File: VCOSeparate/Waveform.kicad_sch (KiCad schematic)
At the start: 27 parts, among them Q1 Q_NPN_ECB, U1 Opamp_Dual, U2 4013, U3 Opamp_Dual

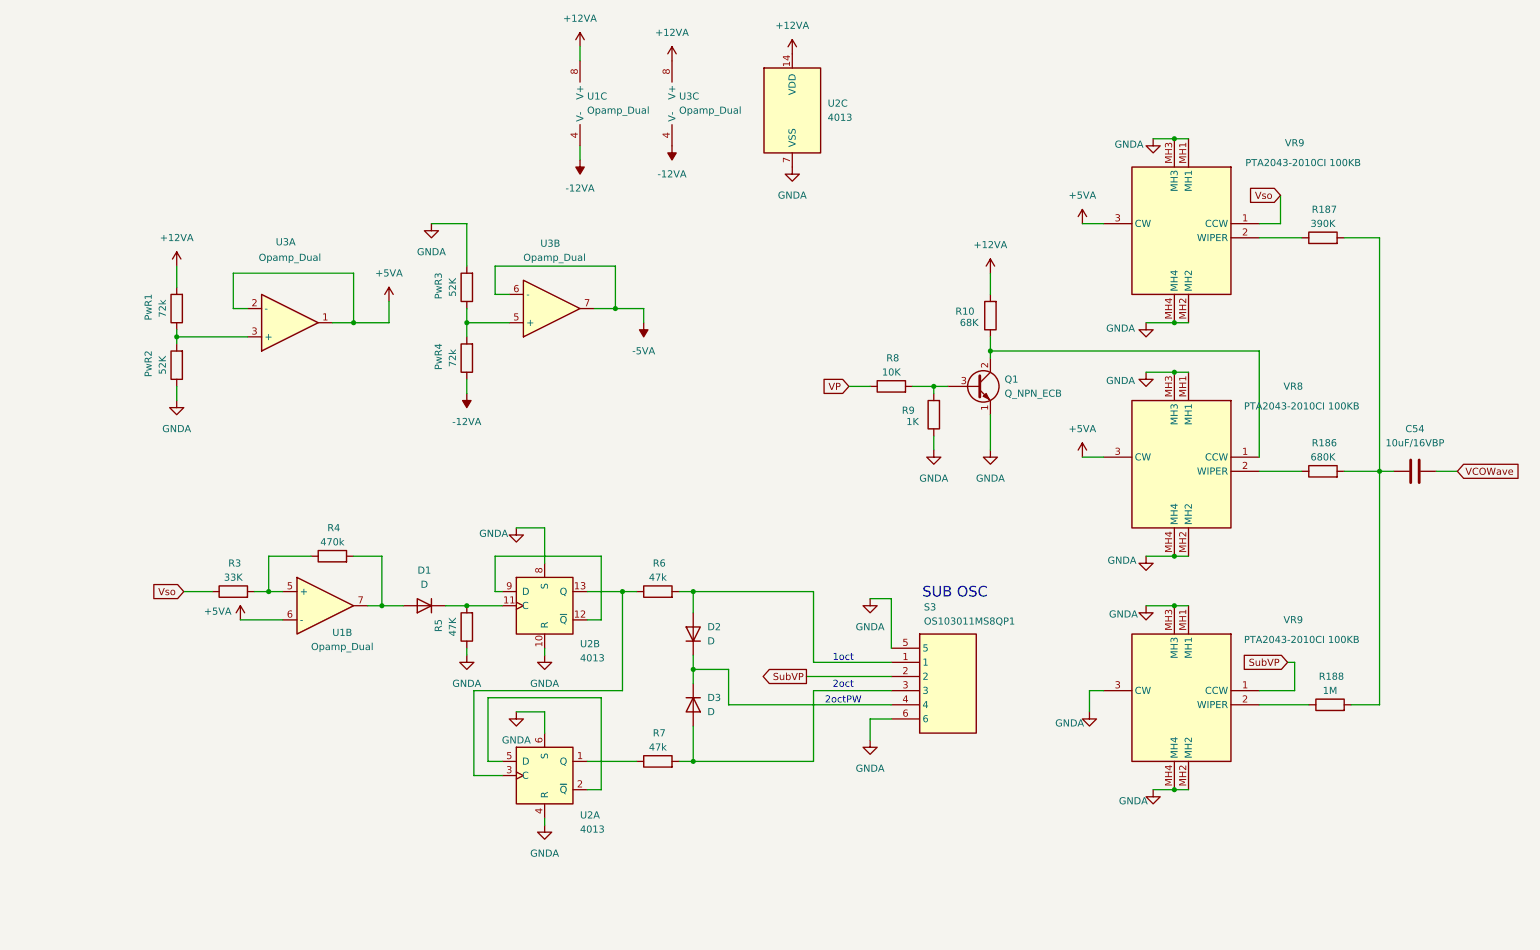
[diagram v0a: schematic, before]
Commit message: MC2
アクセントレベルを追加したEGACCを登録
回路全般部品配置済
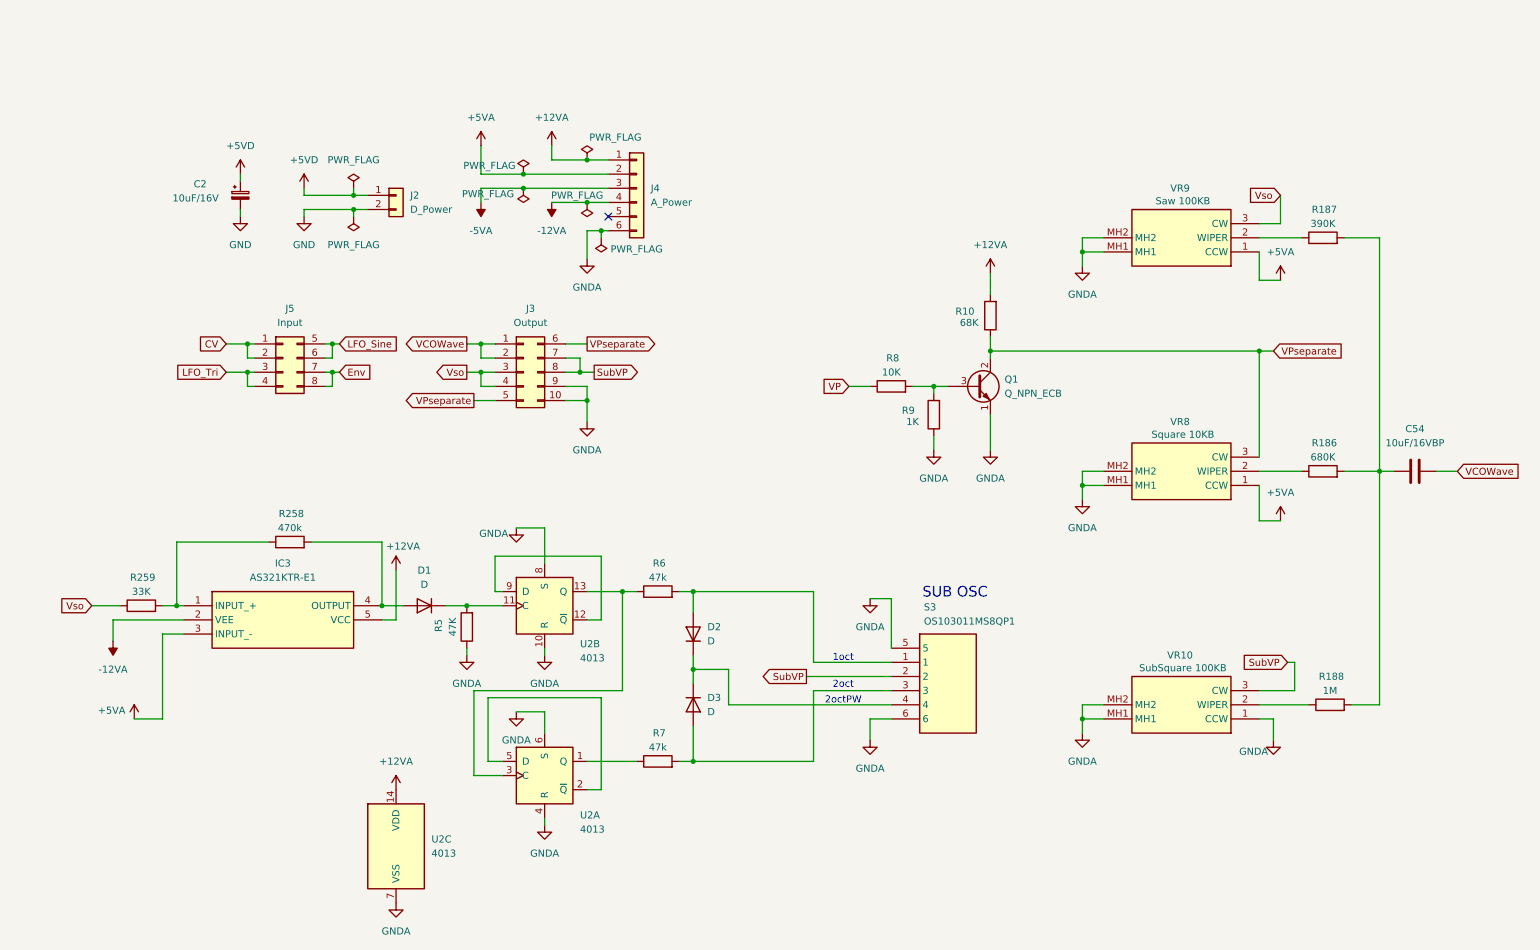
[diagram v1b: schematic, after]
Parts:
- removed PwR1, PwR4: 72k, Resistor_THT:R_Axial_DIN0207_L6.3mm_D2.5mm_P2.54mm_Vertical, symbol Device:R
- removed PwR2, PwR3: 52K, Resistor_THT:R_Axial_DIN0207_L6.3mm_D2.5mm_P2.54mm_Vertical, symbol Device:R
- removed R3: 33K, Resistor_THT:R_Axial_DIN0207_L6.3mm_D2.5mm_P2.54mm_Vertical, symbol Device:R
- removed R4: 470k, Resistor_THT:R_Axial_DIN0207_L6.3mm_D2.5mm_P2.54mm_Vertical, symbol Device:R
- removed U1, U3: Opamp_Dual, Package_DIP:DIP-8_W7.62mm_LongPads, symbol Device:Opamp_Dual
- removed VR8, VR9 (x2): PTA2043-2010CI 100KB, PTA20432010CIB104, symbol SamacSys_Parts:PTA2043-2010CIB104
- added C2: 10uF/16V, Capacitor_THT:CP_Radial_D5.0mm_P2.50mm, symbol Device:C_Polarized_Small
- added IC3: AS321KTR-E1, SOT95P282X145-5N, symbol SamacSys_Parts:AS321KTR-E1
- added J2: D_Power, Connector_PinSocket_2.54mm:PinSocket_1x02_P2.54mm_Vertical, symbol Connector_Generic:Conn_01x02
- added J3: Output, Connector_PinSocket_2.54mm:PinSocket_2x05_P2.54mm_Vertical, symbol Connector_Generic:Conn_02x05_Top_Bottom
- added J4: A_Power, Connector_PinHeader_2.54mm:PinHeader_1x06_P2.54mm_Vertical, symbol Connector_Generic:Conn_01x06
- added J5: Input, Connector_PinSocket_2.54mm:PinSocket_2x04_P2.54mm_Vertical, symbol Connector_Generic:Conn_02x04_Top_Bottom
- added R258: 470k, Resistor_THT:R_Axial_DIN0207_L6.3mm_D2.5mm_P2.54mm_Vertical, symbol Device:R
- added R259: 33K, Resistor_THT:R_Axial_DIN0207_L6.3mm_D2.5mm_P2.54mm_Vertical, symbol Device:R
- added VR10: SubSquare 100KB, SamacSys_Parts:RK09D117000B, symbol SamacSys_Parts:RK09D117000B
- added VR8: Square 10KB, SamacSys_Parts:RK09D117000B, symbol SamacSys_Parts:RK09D117000B
- added VR9: Saw 100KB, SamacSys_Parts:RK09D117000B, symbol SamacSys_Parts:RK09D117000B
- Q1: footprint (none) -> Package_TO_SOT_THT:TO-92_HandSolder
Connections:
- net +12VA: now also IC3.5 (VCC), J4.1 (Pin_1)
- net +5VA: now also IC3.3 (INPUT_-), J4.2 (Pin_2), VR8.1 (CCW), VR9.1 (CCW)
- net -12VA: now also IC3.2 (VEE), J4.4 (Pin_4)
- net -5VA: now also J4.3 (Pin_3)
- net GNDA: now also J3.10 (Pin_10), J3.9 (Pin_9), J4.6 (Pin_6), VR10.1 (CCW), VR10.MH1, VR10.MH2, VR8.MH1, VR8.MH2, VR9.MH1, VR9.MH2
- net SubVP: now also J3.7 (Pin_7), J3.8 (Pin_8), VR10.3 (CW)
- net VCOWave: now also J3.1 (Pin_1), J3.2 (Pin_2)
- net Vso: now also J3.3 (Pin_3), J3.4 (Pin_4), R259.1, VR9.3 (CW)
- net at D1.2 (A): now also IC3.4 (OUTPUT), R258.2
- net VPseparate: now reaches Q1.2 (C), R10.1
- net VPseparate: now also J3.5 (Pin_5), J3.6 (Pin_6), VR8.3 (CW)
- net at R186.1: now also VR8.2 (WIPER)
- net at R188.1: now also VR10.2 (WIPER)
- net at R187.1: now also VR9.2 (WIPER)
- new net: IC3.1 (INPUT_+), R258.1, R259.2
- new net +5VD: C2.1, J2.1 (Pin_1)
- new net CV: J5.1 (Pin_1), J5.2 (Pin_2)
- new net Env: J5.7 (Pin_7), J5.8 (Pin_8)
- new net GND: C2.2, J2.2 (Pin_2)
- new net LFO_Sine: J5.5 (Pin_5), J5.6 (Pin_6)
- new net LFO_Tri: J5.3 (Pin_3), J5.4 (Pin_4)
- no-connect marks 0 -> 1
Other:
- moved on the sheet: U2C

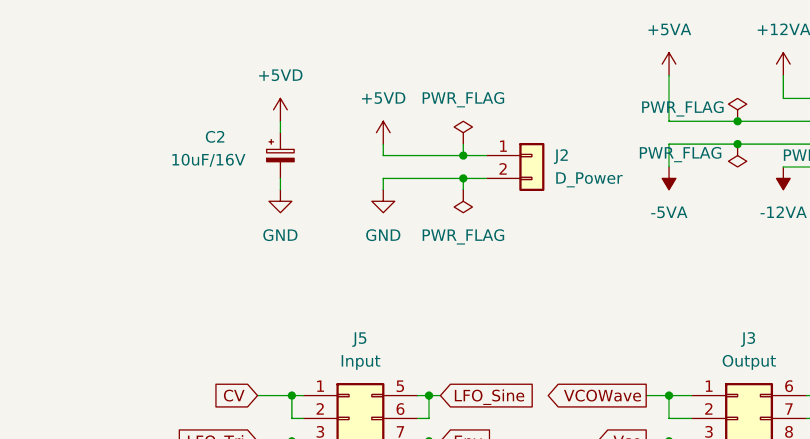
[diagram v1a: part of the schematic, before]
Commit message: MC2
VCO,VCF+VCA,Powerを登録
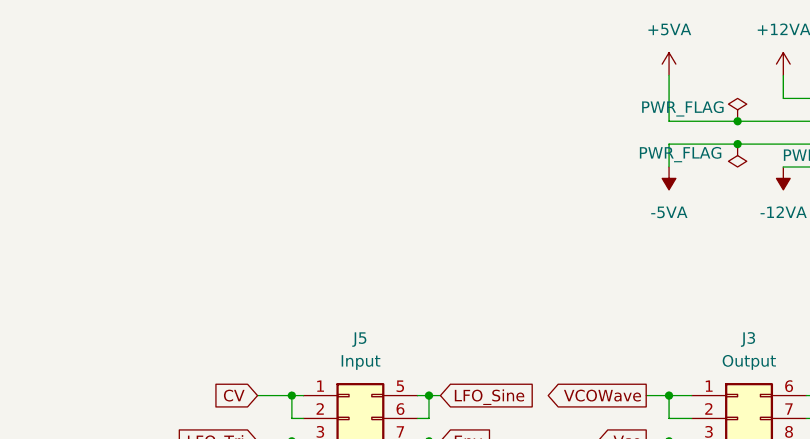
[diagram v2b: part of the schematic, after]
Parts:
- removed C2: 10uF/16V, Capacitor_THT:CP_Radial_D5.0mm_P2.50mm, symbol Device:C_Polarized_Small
- removed J2: D_Power, Connector_PinSocket_2.54mm:PinSocket_1x02_P2.54mm_Vertical, symbol Connector_Generic:Conn_01x02

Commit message: MC2
ここまででFIXした内容
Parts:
- removed Q1: Q_NPN_ECB, Package_TO_SOT_THT:TO-92_HandSolder, symbol Device:Q_NPN_ECB
- added Q18: Q_NPN_ECB, Package_TO_SOT_THT:TO-92_HandSolder, symbol Transistor_BJT:Q_NPN_ECB
- C54: footprint Capacitor_THT:C_Radial_D4.0mm_H7.0mm_P1.50mm -> Capacitor_THT:C_Radial_D6.3mm_H7.0mm_P2.50mm
- IC3: footprint SOT95P282X145-5N -> SamacSys_parts:SOT95P282X145-5N
- S3: footprint OS103011MS8QP1 -> SamacSys_parts:OS103011MS8QP1
- VR10, VR8, VR9: footprint SamacSys_Parts:RK09D117000B -> SamacSys_parts:RK09D117000B
- renumbered D1 to D28, D3 to D31, D2 to D32, U2 to IC4, R5 to R123, R10 to R124, R8 to R128, R9 to R129, R7 to R189, R6 to R190
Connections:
- net GNDA: now also Q18.1 (E)
- net VPseparate: now also Q18.2 (C)
- net at R128.2, R129.2: now also Q18.3 (B)

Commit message: MC2
デバッグ一通り完了して動作出来た
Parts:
- removed J3: Output, Connector_PinSocket_2.54mm:PinSocket_2x05_P2.54mm_Vertical, symbol Connector_Generic:Conn_02x05_Top_Bottom
- added J1: SyncIn, Connector_PinSocket_2.54mm:PinSocket_2x03_P2.54mm_Vertical, symbol Connector_Generic:Conn_02x03_Odd_Even
- added J2: Output, Connector_PinSocket_2.54mm:PinSocket_2x06_P2.54mm_Vertical, symbol Connector_Generic:Conn_02x06_Odd_Even
- added J3: LFM Wave, Connector_PinSocket_2.54mm:PinSocket_2x03_P2.54mm_Vertical, symbol Connector_Generic:Conn_02x03_Odd_Even
- added R3: 390K, Resistor_THT:R_Axial_DIN0207_L6.3mm_D2.5mm_P2.54mm_Vertical, symbol Device:R
- added S1: LFM In, SS14D0839VG5PA, symbol SamacSys_Parts:SS14D0839VG5PA
- added VR1: Tri 100KB, SamacSys_parts:RK09D117000B, symbol SamacSys_Parts:RK09D117000B
- R186: value 680K -> 470K
- R187: value 390K -> 470K
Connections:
- net +5VA: now also VR1.1 (CCW)
- net GNDA: now also J1.3 (Pin_3), J1.4 (Pin_4), J2.11 (Pin_11), J2.12 (Pin_12), S1.5, S1.MH1, S1.MH2, VR1.MH1, VR1.MH2
- net SubVP: now also J2.7 (Pin_7), J2.8 (Pin_8)
- net VCOWave: now also J2.1 (Pin_1), J2.2 (Pin_2)
- net VP: now also J3.3 (Pin_3)
- net VPseparate: now also J2.5 (Pin_5), J2.6 (Pin_6)
- net Vso: now also J2.3 (Pin_3), J2.4 (Pin_4), J3.1 (Pin_1)
- net at C54.1, R186.2, R187.2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: now also R3.2
- new net: R3.1, VR1.2 (WIPER)
- new net: J3.2 (Pin_2), S1.1
- new net: J3.4 (Pin_4), S1.2
- new net: J3.6 (Pin_6), S1.4
- new net HardSyncIn: J1.1 (Pin_1), J1.2 (Pin_2)
- new net LFM_In: S1.3
- new net SoftSyncIn: J1.5 (Pin_5), J1.6 (Pin_6)
- new net Vtri: J2.10 (Pin_10), J2.9 (Pin_9), J3.5 (Pin_5), VR1.3 (CW)
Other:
- moved on the sheet: J4, J5, R188, VR10
